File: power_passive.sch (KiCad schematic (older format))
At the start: 39 parts, among them J10 Conn_01x02, J11 Conn_01x02, J12 Conn_01x02, J13 Conn_01x02, J14 Conn_01x02, J15 Conn_01x02, J16 Conn_01x02, J17 Conn_01x02, J19 Conn_01x02, J21 Conn_01x02, J23 Conn_01x02, J25 Conn_01x02, J27 Conn_01x02, J7 Conn_01x02, J8 ATX-24, J9 Conn_01x02, Q11 MMBT4401-7-F, Q12 MMBT4401-7-F, Q13 SI7113ADN-T1-GE3, Q14 SI7113ADN-T1-GE3, Q15 MMBT4401-7-F, Q16 MMBT4401-7-F, Q17 SI7113ADN-T1-GE3, Q18 SI7113ADN-T1-GE3, Q19 MMBT4401-7-F, Q20 SI7113ADN-T1-GE3, Q21 MMBT4401-7-F

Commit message: Almost
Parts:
- removed J19: Conn_01x02, Connector_Molex:Molex_Micro-Fit_3.0_43045-0212_2x01_P3.00mm_Vertical, symbol Connector_Generic:Conn_01x02
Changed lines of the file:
@@
-	1    0    0    -1
-$EndComp
-Wire Wire Line
-	8150 2000 8000 2000
-Wire Wire Line
-	8000 2000 8000 1900
-Wire Wire Line
-	8150 2100 8000 2100
-Wire Wire Line
-	8000 2100 8000 2200
-$Comp
-L power:GND #PWR?
-U 1 1 5E41B364
-P 8000 2200
-AR Path="/5E41B364" Ref="#PWR?"  Part="1"
-AR Path="/5E4060AB/5E41B364" Ref="#PWR0160"  Part="1"
-F 0 "#PWR0160" H 8000 1950 50  0001 C CNN
-F 1 "GND" H 8005 2027 50  0000 C CNN
-F 2 "" H 8000 2200 50  0001 C CNN
-F 3 "" H 8000 2200 50  0001 C CNN
-	1    8000 2200
-	1    0    0    -1
-$EndComp
-$Comp
-L power:+3V3 #PWR?
-U 1 1 5E41B374
-P 8000 1900
-AR Path="/5E41B374" Ref="#PWR?"  Part="1"
-AR Path="/5E4060AB/5E41B374" Ref="#PWR0162"  Part="1"
-F 0 "#PWR0162" H 8000 1750 50  0001 C CNN
-F 1 "+3V3" H 8015 2073 50  0000 C CNN
-F 2 "" H 8000 1900 50  0001 C CNN
-F 3 "" H 8000 1900 50  0001 C CNN
-	1    8000 1900
 	1    0    0    -1
 $EndComp
 $Comp
 L Connector_Generic:Conn_01x02 J?
-U 1 1 5E41B388
-P 8350 2000
-AR Path="/5E41B388" Ref="J?"  Part="1"
-AR Path="/5E4060AB/5E41B388" Ref="J19"  Part="1"
-F 0 "J19" H 8430 1992 50  0000 L CNN
-F 1 "Conn_01x02" H 8430 1901 50  0000 L CNN
-F 2 "Connector_Molex:Molex_Micro-Fit_3.0_43045-0212_2x01_P3.00mm_Vertical" H 8350 2000 50  0001 C CNN
-F 3 "~" H 8350 2000 50  0001 C CNN
-F 4 "43045-0212" H 8350 2000 50  0001 C CNN "manf#"
-	1    8350 2000
-	1    0    0    -1
-$EndComp
-$Comp
-L Connector_Generic:Conn_01x02 J?

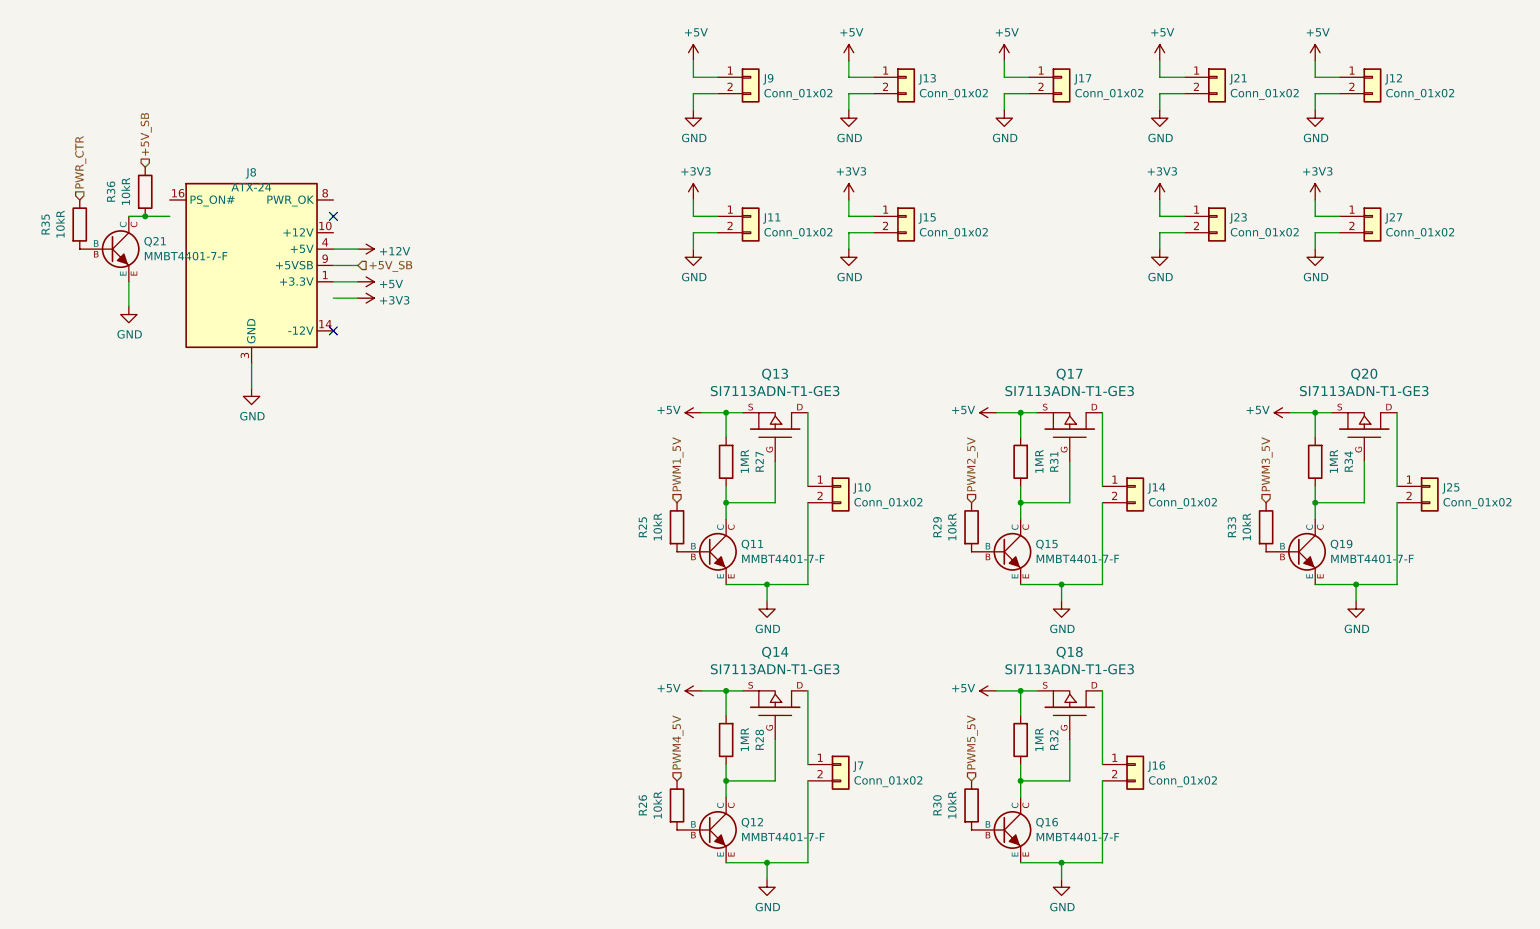
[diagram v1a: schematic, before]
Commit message: Positioning finished
Lacks fine alignment.
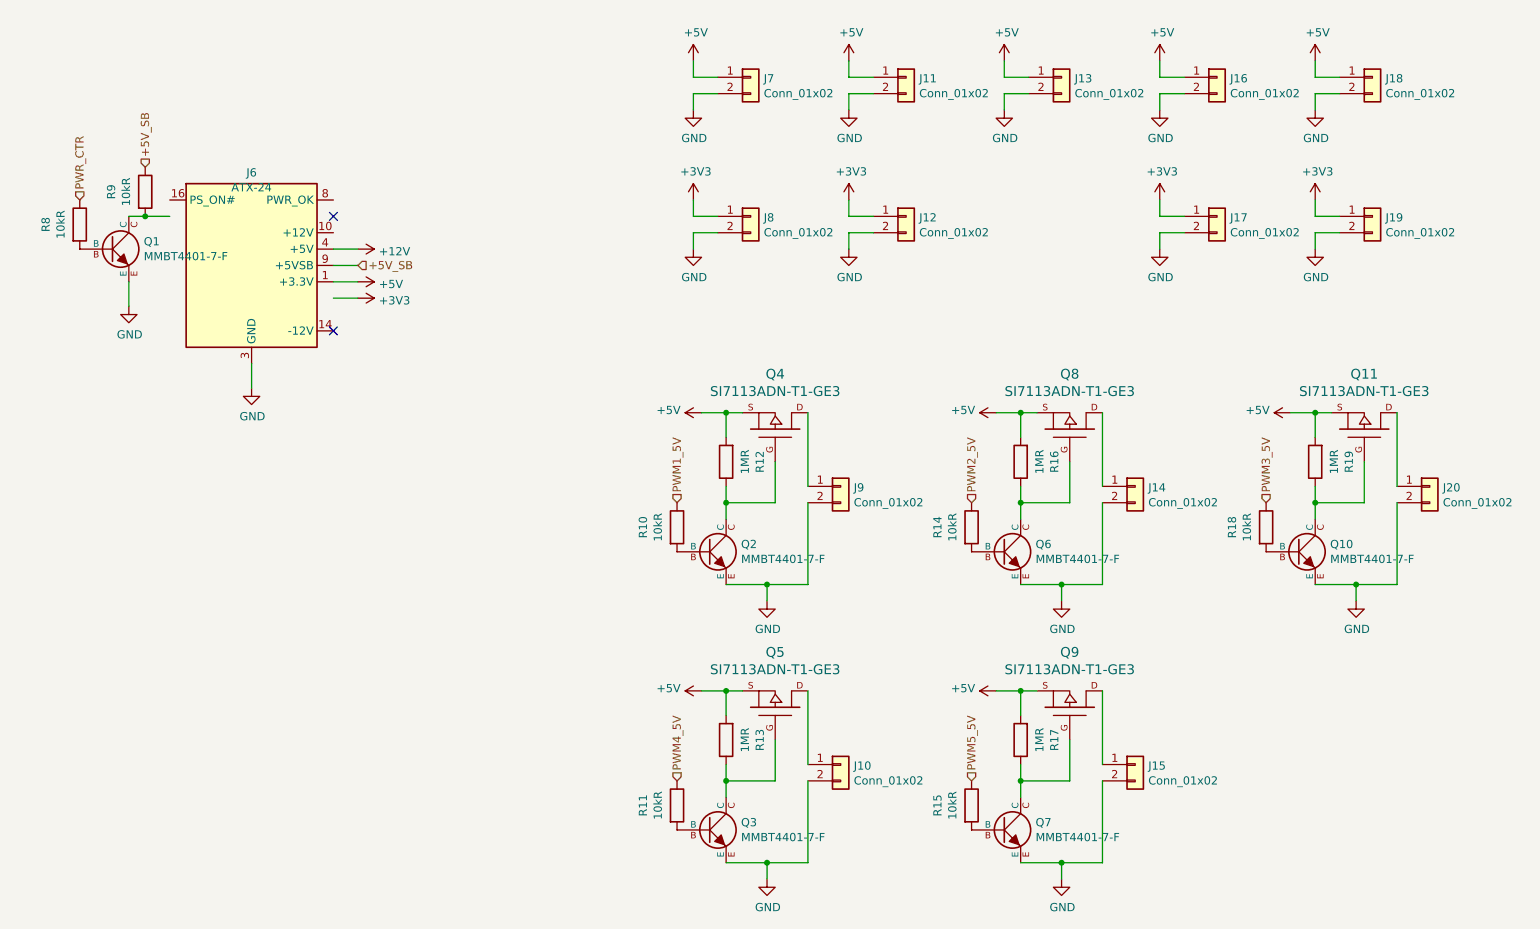
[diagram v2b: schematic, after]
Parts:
- renumbered J7 to J10, J13 to J11, J15 to J12, J17 to J13, J16 to J15, J21 to J16, J23 to J17, J12 to J18, J27 to J19, J25 to J20, J8 to J6, J9 to J7, J11 to J8, J10 to J9, Q21 to Q1, Q19 to Q10, Q20 to Q11, Q11 to Q2, Q12 to Q3, Q13 to Q4, Q14 to Q5, Q15 to Q6, Q16 to Q7, Q17 to Q8, Q18 to Q9, R25 to R10, R26 to R11, R27 to R12, R28 to R13, R29 to R14, R30 to R15, R31 to R16, R32 to R17, R33 to R18, R34 to R19, R35 to R8, R36 to R9

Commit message: Start MCU layout
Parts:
- added J14: Conn_01x02, Connector_Molex:Molex_Micro-Fit_3.0_43045-0212_2x01_P3.00mm_Vertical, symbol Connector_Generic:Conn_01x02
- renumbered J14 to J15, J15 to J16, J16 to J17, J17 to J18, J18 to J19, J19 to J20, J20 to J21
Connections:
- net +3V3: now also J14.1 (Pin_1)
- net GND: now also J14.2 (Pin_2)

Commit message: Stash
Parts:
- renumbered J11 to J10, J12 to J11, J13 to J12, J14 to J13, J15 to J14, J16 to J15, J17 to J16, J18 to J17, J19 to J18, J20 to J19, J21 to J20, J6 to J5, J7 to J6, J8 to J7, J9 to J8, J10 to J9
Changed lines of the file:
@@
 P 6450 1150
 AR Path="/5E41B282" Ref="J?"  Part="1"
-AR Path="/5E4060AB/5E41B282" Ref="J7"  Part="1"
-F 0 "J7" H 6530 1142 50  0000 L CNN
+AR Path="/5E4060AB/5E41B282" Ref="J6"  Part="1"
+F 0 "J6" H 6530 1142 50  0000 L CNN
 F 1 "Conn_01x02" H 6530 1051 50  0000 L CNN
 F 2 "Connector_Molex:Molex_Micro-Fit_3.0_43045-0212_2x01_P3.00mm_Vertical" H 6450 1150 50  0001 C CNN
@@
 P 7000 3650
 AR Path="/5E41B2C9" Ref="J?"  Part="1"
-AR Path="/5E4060AB/5E41B2C9" Ref="J9"  Part="1"
-F 0 "J9" H 7080 3642 50  0000 L CNN
+AR Path="/5E4060AB/5E41B2C9" Ref="J8"  Part="1"
+F 0 "J8" H 7080 3642 50  0000 L CNN
 F 1 "Conn_01x02" H 7080 3551 50  0000 L CNN
 F 2 "Connector_Molex:Molex_Micro-Fit_3.0_43045-0212_2x01_P3.00mm_Vertical" H 7000 3650 50  0001 C CNN
@@
 P 6450 2000
 AR Path="/5E41B2D0" Ref="J?"  Part="1"
-AR Path="/5E4060AB/5E41B2D0" Ref="J8"  Part="1"
-F 0 "J8" H 6530 1992 50  0000 L CNN
+AR Path="/5E4060AB/5E41B2D0" Ref="J7"  Part="1"
+F 0 "J7" H 6530 1992 50  0000 L CNN
 F 1 "Conn_01x02" H 6530 1901 50  0000 L CNN
 F 2 "Connector_Molex:Molex_Micro-Fit_3.0_43045-0212_2x01_P3.00mm_Vertical" H 6450 2000 50  0001 C CNN
@@
 P 7400 1150
 AR Path="/5E41B2DE" Ref="J?"  Part="1"
-AR Path="/5E4060AB/5E41B2DE" Ref="J11"  Part="1"
-F 0 "J11" H 7480 1142 50  0000 L CNN
+AR Path="/5E4060AB/5E41B2DE" Ref="J10"  Part="1"
+F 0 "J10" H 7480 1142 50  0000 L CNN
 F 1 "Conn_01x02" H 7480 1051 50  0000 L CNN
 F 2 "Connector_Molex:Molex_Micro-Fit_3.0_43045-0212_2x01_P3.00mm_Vertical" H 7400 1150 50  0001 C CNN
@@
 P 7400 2000
 AR Path="/5E41B32C" Ref="J?"  Part="1"
-AR Path="/5E4060AB/5E41B32C" Ref="J12"  Part="1"
-F 0 "J12" H 7480 1992 50  0000 L CNN
+AR Path="/5E4060AB/5E41B32C" Ref="J11"  Part="1"
+F 0 "J11" H 7480 1992 50  0000 L CNN
 F 1 "Conn_01x02" H 7480 1901 50  0000 L CNN
 F 2 "Connector_Molex:Molex_Micro-Fit_3.0_43045-0212_2x01_P3.00mm_Vertical" H 7400 2000 50  0001 C CNN
@@
 P 8350 1150
 AR Path="/5E41B33A" Ref="J?"  Part="1"
-AR Path="/5E4060AB/5E41B33A" Ref="J13"  Part="1"
-F 0 "J13" H 8430 1142 50  0000 L CNN
+AR Path="/5E4060AB/5E41B33A" Ref="J12"  Part="1"
+F 0 "J12" H 8430 1142 50  0000 L CNN
 F 1 "Conn_01x02" H 8430 1051 50  0000 L CNN
 F 2 "Connector_Molex:Molex_Micro-Fit_3.0_43045-0212_2x01_P3.00mm_Vertical" H 8350 1150 50  0001 C CNN
@@
 P 9300 1150
 AR Path="/5E41B396" Ref="J?"  Part="1"
-AR Path="/5E4060AB/5E41B396" Ref="J17"  Part="1"
-F 0 "J17" H 9380 1142 50  0000 L CNN
+AR Path="/5E4060AB/5E41B396" Ref="J16"  Part="1"
+F 0 "J16" H 9380 1142 50  0000 L CNN
 F 1 "Conn_01x02" H 9380 1051 50  0000 L CNN
 F 2 "Connector_Molex:Molex_Micro-Fit_3.0_43045-0212_2x01_P3.00mm_Vertical" H 9300 1150 50  0001 C CNN
@@
 P 9300 2000
 AR Path="/5E41B3E4" Ref="J?"  Part="1"
-AR Path="/5E4060AB/5E41B3E4" Ref="J18"  Part="1"
-F 0 "J18" H 9380 1992 50  0000 L CNN
+AR Path="/5E4060AB/5E41B3E4" Ref="J17"  Part="1"
+F 0 "J17" H 9380 1992 50  0000 L CNN
 F 1 "Conn_01x02" H 9380 1901 50  0000 L CNN
 F 2 "Connector_Molex:Molex_Micro-Fit_3.0_43045-0212_2x01_P3.00mm_Vertical" H 9300 2000 50  0001 C CNN
@@
 P 10250 2000
 AR Path="/5E41B440" Ref="J?"  Part="1"
-AR Path="/5E4060AB/5E41B440" Ref="J20"  Part="1"
-F 0 "J20" H 10330 1992 50  0000 L CNN
+AR Path="/5E4060AB/5E41B440" Ref="J19"  Part="1"
+F 0 "J19" H 10330 1992 50  0000 L CNN
 F 1 "Conn_01x02" H 10330 1901 50  0000 L CNN
 F 2 "Connector_Molex:Molex_Micro-Fit_3.0_43045-0212_2x01_P3.00mm_Vertical" H 10250 2000 50  0001 C CNN
@@
 +5V_SB
 $Comp
-L Connector:ATX-24 J6
+L Connector:ATX-24 J5
 U 1 1 5E29B35F
 P 3400 2300
-F 0 "J6" H 3400 2867 50  0000 C CNN
+F 0 "J5" H 3400 2867 50  0000 C CNN
 F 1 "ATX-24" H 3400 2776 50  0000 C CNN
 F 2 "Connector_Molex:Molex_Mini-Fit_Jr_5566-24A_2x12_P4.20mm_Vertical" H 3400 2200 50  0001 C CNN
@@
 P 10250 1150
 AR Path="/5E3EAC7E" Ref="J?"  Part="1"
-AR Path="/5E4060AB/5E3EAC7E" Ref="J19"  Part="1"
-F 0 "J19" H 10330 1142 50  0000 L CNN
+AR Path="/5E4060AB/5E3EAC7E" Ref="J18"  Part="1"
+F 0 "J18" H 10330 1142 50  0000 L CNN
 F 1 "Conn_01x02" H 10330 1051 50  0000 L CNN
 F 2 "Connector_Molex:Molex_Micro-Fit_3.0_43045-0212_2x01_P3.00mm_Vertical" H 10250 1150 50  0001 C CNN
@@
 P 8800 3650
 AR Path="/5E726264" Ref="J?"  Part="1"
-AR Path="/5E4060AB/5E726264" Ref="J15"  Part="1"
-F 0 "J15" H 8880 3642 50  0000 L CNN
+AR Path="/5E4060AB/5E726264" Ref="J14"  Part="1"
+F 0 "J14" H 8880 3642 50  0000 L CNN
 F 1 "Conn_01x02" H 8880 3551 50  0000 L CNN
 F 2 "Connector_Molex:Molex_Micro-Fit_3.0_43045-0212_2x01_P3.00mm_Vertical" H 8800 3650 50  0001 C CNN
@@
 P 10600 3650
 AR Path="/5E74047D" Ref="J?"  Part="1"
-AR Path="/5E4060AB/5E74047D" Ref="J21"  Part="1"
-F 0 "J21" H 10680 3642 50  0000 L CNN
+AR Path="/5E4060AB/5E74047D" Ref="J20"  Part="1"
+F 0 "J20" H 10680 3642 50  0000 L CNN
 F 1 "Conn_01x02" H 10680 3551 50  0000 L CNN
 F 2 "Connector_Molex:Molex_Micro-Fit_3.0_43045-0212_2x01_P3.00mm_Vertical" H 10600 3650 50  0001 C CNN
@@
 P 7000 5350
 AR Path="/5E7404BA" Ref="J?"  Part="1"
-AR Path="/5E4060AB/5E7404BA" Ref="J10"  Part="1"
-F 0 "J10" H 7080 5342 50  0000 L CNN
+AR Path="/5E4060AB/5E7404BA" Ref="J9"  Part="1"
+F 0 "J9" H 7080 5342 50  0000 L CNN
 F 1 "Conn_01x02" H 7080 5251 50  0000 L CNN
 F 2 "Connector_Molex:Molex_Micro-Fit_3.0_43045-0212_2x01_P3.00mm_Vertical" H 7000 5350 50  0001 C CNN
@@
 P 8800 5350
 AR Path="/5E753385" Ref="J?"  Part="1"
-AR Path="/5E4060AB/5E753385" Ref="J16"  Part="1"
-F 0 "J16" H 8880 5342 50  0000 L CNN
+AR Path="/5E4060AB/5E753385" Ref="J15"  Part="1"
+F 0 "J15" H 8880 5342 50  0000 L CNN
 F 1 "Conn_01x02" H 8880 5251 50  0000 L CNN
 F 2 "Connector_Molex:Molex_Micro-Fit_3.0_43045-0212_2x01_P3.00mm_Vertical" H 8800 5350 50  0001 C CNN
@@
 P 8350 2000
 AR Path="/5E408355" Ref="J?"  Part="1"
-AR Path="/5E4060AB/5E408355" Ref="J14"  Part="1"
-F 0 "J14" H 8430 1992 50  0000 L CNN
+AR Path="/5E4060AB/5E408355" Ref="J13"  Part="1"
+F 0 "J13" H 8430 1992 50  0000 L CNN
 F 1 "Conn_01x02" H 8430 1901 50  0000 L CNN
 F 2 "Connector_Molex:Molex_Micro-Fit_3.0_43045-0212_2x01_P3.00mm_Vertical" H 8350 2000 50  0001 C CNN

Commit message: ICs positioning
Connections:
- net PWM2_5V: now also R11.1; no longer R14.1
- net PWM3_5V: now also R14.1; no longer R18.1
- net PWM4_5V: now also R15.1; no longer R11.1
- net PWM5_5V: now also R18.1; no longer R15.1
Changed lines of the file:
@@
 	8100 3200 7950 3200
 Connection ~ 8100 3200
-Text HLabel 7800 3750 1    50   Input ~ 0
+Text HLabel 6000 5450 1    50   Input ~ 0
 PWM2_5V
 $Comp
@@
 	9900 3200 9750 3200
 Connection ~ 9900 3200
-Text HLabel 9600 3750 1    50   Input ~ 0
+Text HLabel 7800 3750 1    50   Input ~ 0
 PWM3_5V
 $Comp
@@
 	6300 4900 6150 4900
 Connection ~ 6300 4900
-Text HLabel 6000 5450 1    50   Input ~ 0
+Text HLabel 7800 5450 1    50   Input ~ 0
 PWM4_5V
 $Comp
@@
 	8100 4900 7950 4900
 Connection ~ 8100 4900
-Text HLabel 7800 5450 1    50   Input ~ 0
+Text HLabel 9600 3750 1    50   Input ~ 0
 PWM5_5V
 $Comp

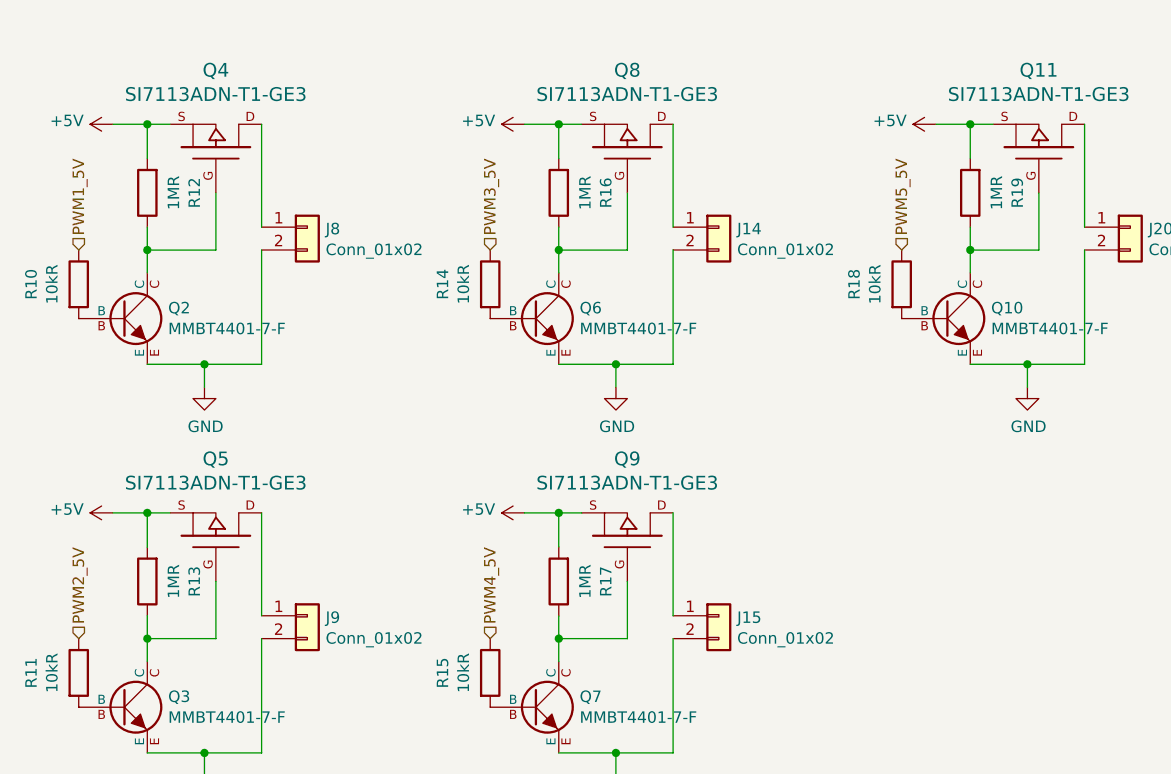
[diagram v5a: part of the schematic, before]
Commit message: Added remaining 0603 references
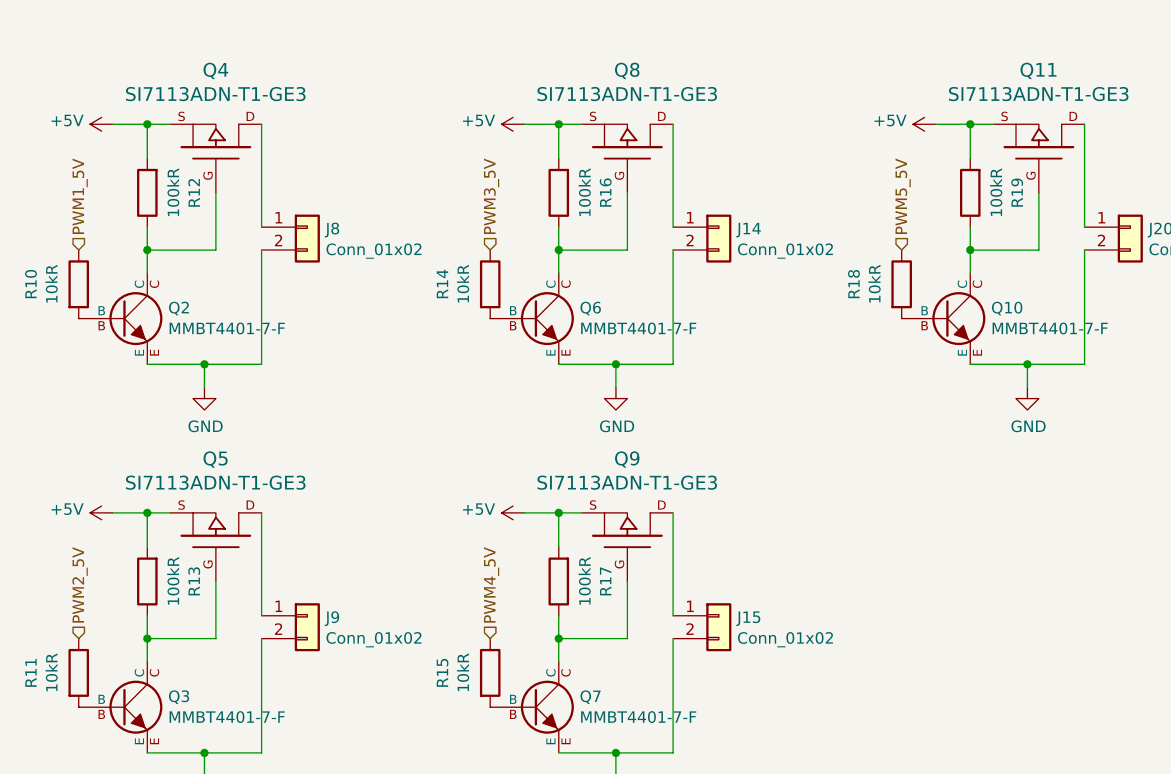
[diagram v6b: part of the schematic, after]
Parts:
- R10, R11, R14, R15, R18, R8, R9: manf# (none) -> CRCW060310K0JNEBC
- R12, R13, R16, R17, R19: value 1MR -> 100kR; manf# (none) -> CRCW0603100KFKEAC
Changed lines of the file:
@@
 F 2 "lsts-passives:R_0603" V 5930 3900 50  0001 C CNN
 F 3 "~" H 6000 3900 50  0001 C CNN
+F 4 "CRCW060310K0JNEBC" H 6000 3900 50  0001 C CNN "manf#"
 	1    6000 3900
 	1    0    0    -1
@@
 AR Path="/5E4060AB/5E6D1790" Ref="R12"  Part="1"
 F 0 "R12" V 6093 3500 50  0000 C CNN
-F 1 "1MR" V 6184 3500 50  0000 C CNN
+F 1 "100kR" V 6184 3500 50  0000 C CNN
 F 2 "lsts-passives:R_0603" V 6230 3500 50  0001 C CNN
 F 3 "~" H 6300 3500 50  0001 C CNN
+F 4 "CRCW0603100KFKEAC" H 6300 3500 50  0001 C CNN "manf#"
 	1    6300 3500
 	-1   0    0    1
@@
 F 2 "lsts-passives:R_0603" V 7730 3900 50  0001 C CNN
 F 3 "~" H 7800 3900 50  0001 C CNN
+F 4 "CRCW060310K0JNEBC" H 7800 3900 50  0001 C CNN "manf#"
 	1    7800 3900
 	1    0    0    -1
@@
 AR Path="/5E4060AB/5E72628F" Ref="R16"  Part="1"
 F 0 "R16" V 7893 3500 50  0000 C CNN
-F 1 "1MR" V 7984 3500 50  0000 C CNN
+F 1 "100kR" V 7984 3500 50  0000 C CNN
 F 2 "lsts-passives:R_0603" V 8030 3500 50  0001 C CNN
 F 3 "~" H 8100 3500 50  0001 C CNN
+F 4 "CRCW0603100KFKEAC" H 8100 3500 50  0001 C CNN "manf#"
 	1    8100 3500
 	-1   0    0    1
@@
 F 2 "lsts-passives:R_0603" V 9530 3900 50  0001 C CNN
 F 3 "~" H 9600 3900 50  0001 C CNN
+F 4 "CRCW060310K0JNEBC" H 9600 3900 50  0001 C CNN "manf#"
 	1    9600 3900
 	1    0    0    -1
@@
 AR Path="/5E4060AB/5E7404A8" Ref="R19"  Part="1"
 F 0 "R19" V 9693 3500 50  0000 C CNN
-F 1 "1MR" V 9784 3500 50  0000 C CNN
+F 1 "100kR" V 9784 3500 50  0000 C CNN
 F 2 "lsts-passives:R_0603" V 9830 3500 50  0001 C CNN
 F 3 "~" H 9900 3500 50  0001 C CNN
+F 4 "CRCW0603100KFKEAC" H 9900 3500 50  0001 C CNN "manf#"
 	1    9900 3500
 	-1   0    0    1
@@
 F 2 "lsts-passives:R_0603" V 5930 5600 50  0001 C CNN
 F 3 "~" H 6000 5600 50  0001 C CNN
+F 4 "CRCW060310K0JNEBC" H 6000 5600 50  0001 C CNN "manf#"
 	1    6000 5600
 	1    0    0    -1
@@
 AR Path="/5E4060AB/5E7404E5" Ref="R13"  Part="1"
 F 0 "R13" V 6093 5200 50  0000 C CNN
-F 1 "1MR" V 6184 5200 50  0000 C CNN
+F 1 "100kR" V 6184 5200 50  0000 C CNN
 F 2 "lsts-passives:R_0603" V 6230 5200 50  0001 C CNN
 F 3 "~" H 6300 5200 50  0001 C CNN
+F 4 "CRCW0603100KFKEAC" H 6300 5200 50  0001 C CNN "manf#"
 	1    6300 5200
 	-1   0    0    1
@@
 F 2 "lsts-passives:R_0603" V 7730 5600 50  0001 C CNN
 F 3 "~" H 7800 5600 50  0001 C CNN
+F 4 "CRCW060310K0JNEBC" H 7800 5600 50  0001 C CNN "manf#"
 	1    7800 5600
 	1    0    0    -1
@@
 AR Path="/5E4060AB/5E7533B0" Ref="R17"  Part="1"
 F 0 "R17" V 7893 5200 50  0000 C CNN
-F 1 "1MR" V 7984 5200 50  0000 C CNN
+F 1 "100kR" V 7984 5200 50  0000 C CNN
 F 2 "lsts-passives:R_0603" V 8030 5200 50  0001 C CNN
 F 3 "~" H 8100 5200 50  0001 C CNN
+F 4 "CRCW0603100KFKEAC" H 8100 5200 50  0001 C CNN "manf#"
 	1    8100 5200
 	-1   0    0    1
@@
 F 2 "lsts-passives:R_0603" V 2280 2050 50  0001 C CNN
 F 3 "~" H 2350 2050 50  0001 C CNN
+F 4 "CRCW060310K0JNEBC" H 2350 2050 50  0001 C CNN "manf#"
 	1    2350 2050
 	1    0    0    -1
@@
 F 2 "lsts-passives:R_0603" V 2680 1850 50  0001 C CNN
 F 3 "~" H 2750 1850 50  0001 C CNN
+F 4 "CRCW060310K0JNEBC" H 2750 1850 50  0001 C CNN "manf#"
 	1    2750 1850
 	1    0    0    -1
